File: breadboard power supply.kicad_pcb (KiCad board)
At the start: 2 copper layers, 70.8 x 61.1 mm, 27 parts, among them J1 Screw_Terminal_01x02, J10 Conn_01x03_Male, J11 Barrel_Jack_Switch, J12 Conn_01x02_Male, J13 Screw_Terminal_01x02, J2 USB_B, J3 Conn_01x03_Male, J4 Conn_01x03_Male, J5 Conn_01x02_Male, J6 Conn_01x03_Male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

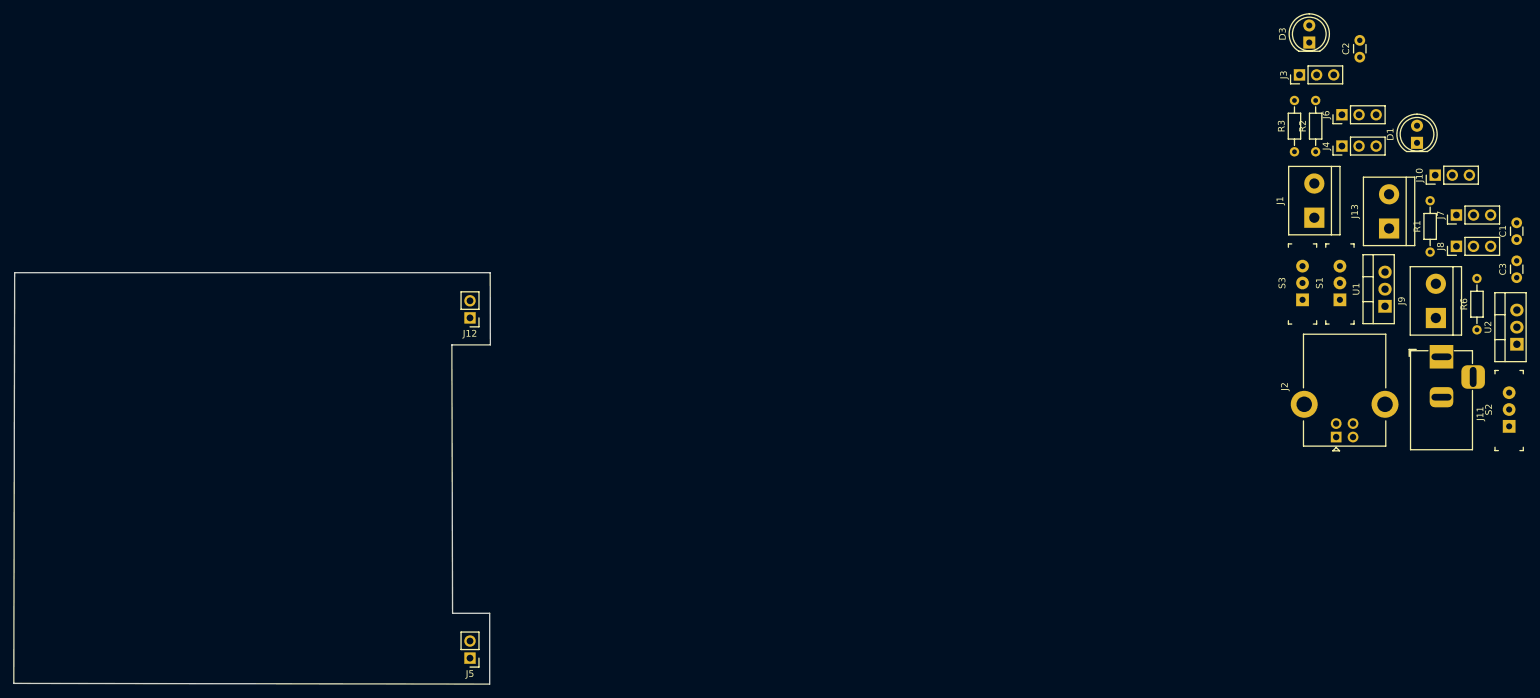
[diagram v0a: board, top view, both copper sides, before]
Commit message: footprints arranged
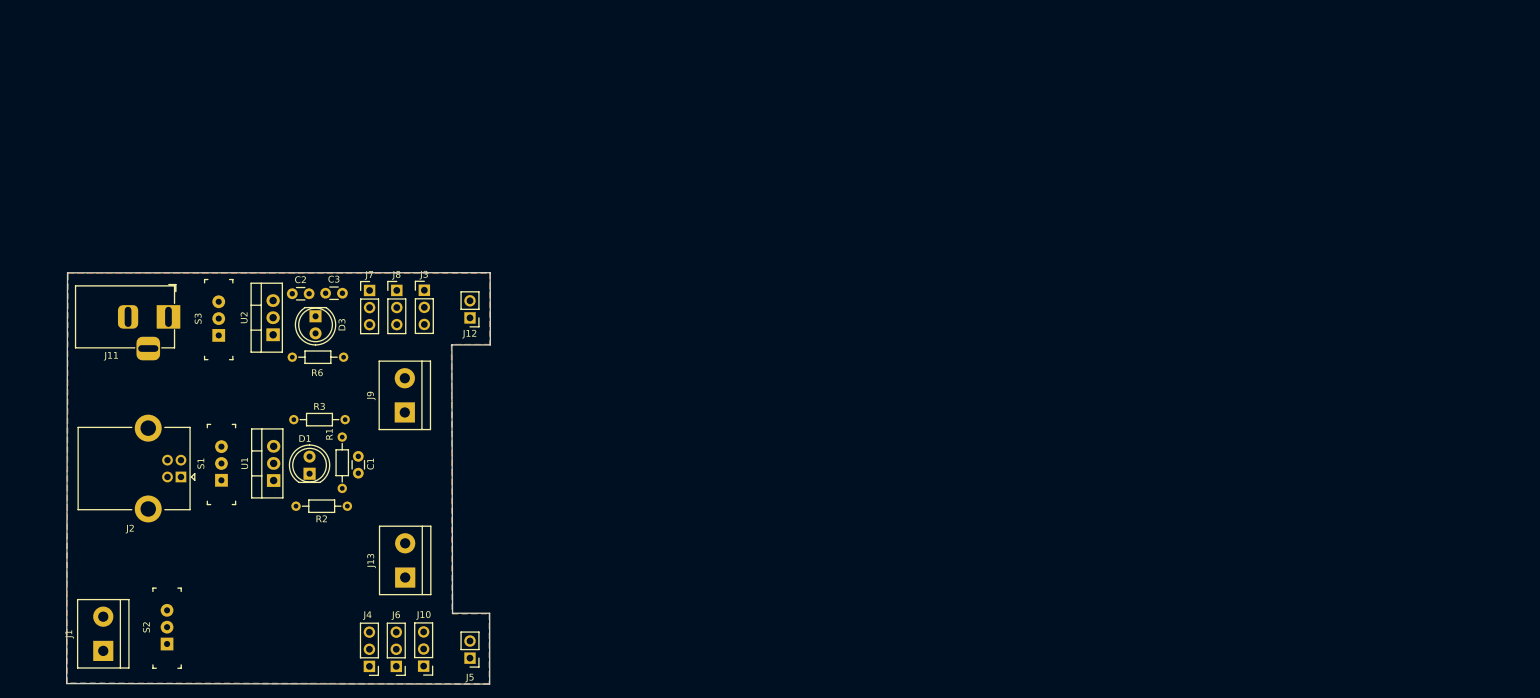
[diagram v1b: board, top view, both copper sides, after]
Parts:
- moved S2 201.9 mm to (165.4, 103.0)
- moved J1 191.0 mm to (155.9, 104.0)
- moved J11 189.1 mm to (165.6, 54.4), turned to 0 degrees
- moved U2 184.7 mm to (181.2, 57.0)
- moved C3 176.9 mm to (188.9, 50.9), turned to 0 degrees
- moved R6 176.0 mm to (184.0, 60.4), turned to 0 degrees
- moved C1 175.5 mm to (193.8, 77.6)
- moved J2 171.6 mm to (167.5, 78.2), turned to 180 degrees
- moved D1 171.6 mm to (186.6, 77.7)
- moved S1 168.2 mm to (173.5, 78.7)
- moved U1 167.0 mm to (181.2, 78.7)
- moved J10 167.0 mm to (203.5, 106.2), turned to 180 degrees
- moved R1 165.3 mm to (191.4, 79.9)
- moved J4 163.8 mm to (195.5, 106.3), turned to 180 degrees
- moved J6 162.6 mm to (199.4, 106.3), turned to 180 degrees
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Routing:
- added copper zone on B.Cu, net GND
- added copper zone on F.Cu, net GND
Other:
- board size 70.8 x 61.1 mm -> 62.9 x 61.1 mm
